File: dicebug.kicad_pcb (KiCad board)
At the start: 2 copper layers, 120.6 x 77.6 mm, 33 parts, among them SW1 SW_SPDT, U1 74LV163ADR, U3 74HCS7266DR, U5 iqs211a

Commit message: mostly done...
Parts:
- BT1: footprint Battery:BatteryHolder_Keystone_3034_1x20mm -> sensors:bh-3034-74-combined
- D1, D2, D3, D4, D5, D6, D7: footprint proj_footprints:PointLED_reverse_mount -> proj_footprints:PointLED_reverse_mount_bigger_pads
- TP2, TP3, TP4: footprint TestPoint:TestPoint_Pad_D2.0mm -> TestPoint:TestPoint_Pad_D1.0mm
- moved TP3 137.8 mm to (90.7, 100.3)
- moved TP2 119.2 mm to (108.6, 102.5)
- moved TP1 57.0 mm to (116.5, 95.2)
- moved TP4 42.9 mm to (92.5, 112.1)
- moved R1 5.16 mm to (93.0, 97.1), turned to 90 degrees
- moved R4 2.28 mm to (112.8, 95.2)
- moved BT1 1.25 mm to (100.1, 87.2), turned to 0 degrees
- moved C1 0.12 mm to (95.9, 103.0)
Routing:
- net GND: track 146.3 -> 186.6 mm
- net Net-(BT1-+): track 50.7 -> 70.2 mm
- net Net-(D1-A): track 3.85 -> 10.4 mm
- net Net-(U5-IO1/SCL): track 0.00 -> 5.26 mm
- net Net-(R4-Pad1): track 80.8 -> 76.5 mm
- net Net-(U1-Q0): track 38.4 -> 42.0 mm
- net Net-(R6-Pad1): track 42.9 -> 44.6 mm
- net +3V0: track 58.0 -> 59.3 mm
- net Net-(D4-A): track 3.05 -> 1.86 mm
- net Net-(R2-Pad1): track 83.4 -> 84.5 mm
- net Net-(U1-CP): track 15.0 -> 15.7 mm
- removed copper zone on B.Cu, net (none)
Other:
- board size 120.6 x 77.6 mm -> 47.8 x 48.5 mm
- board text added: "JLCJLCJLCJLC"

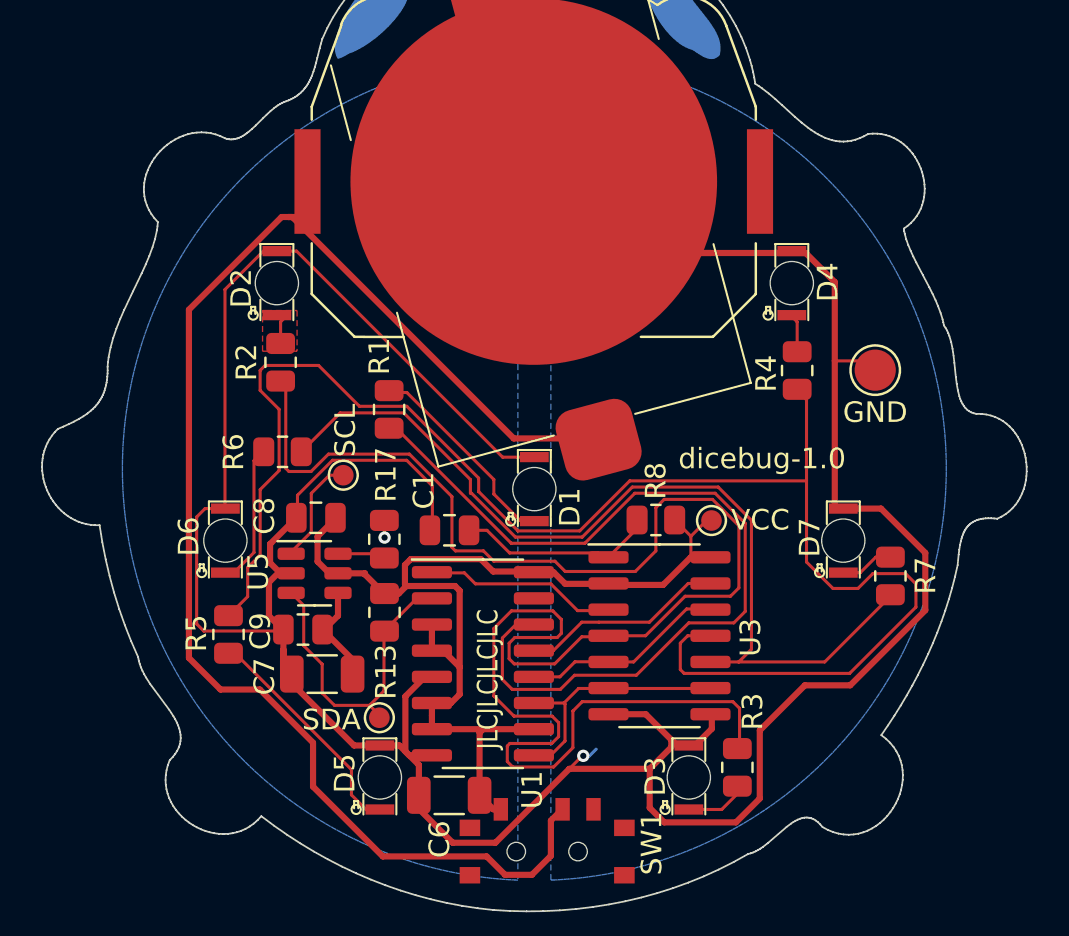
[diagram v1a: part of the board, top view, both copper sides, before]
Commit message: updated part values, numbers/id and manufacturers; added comments
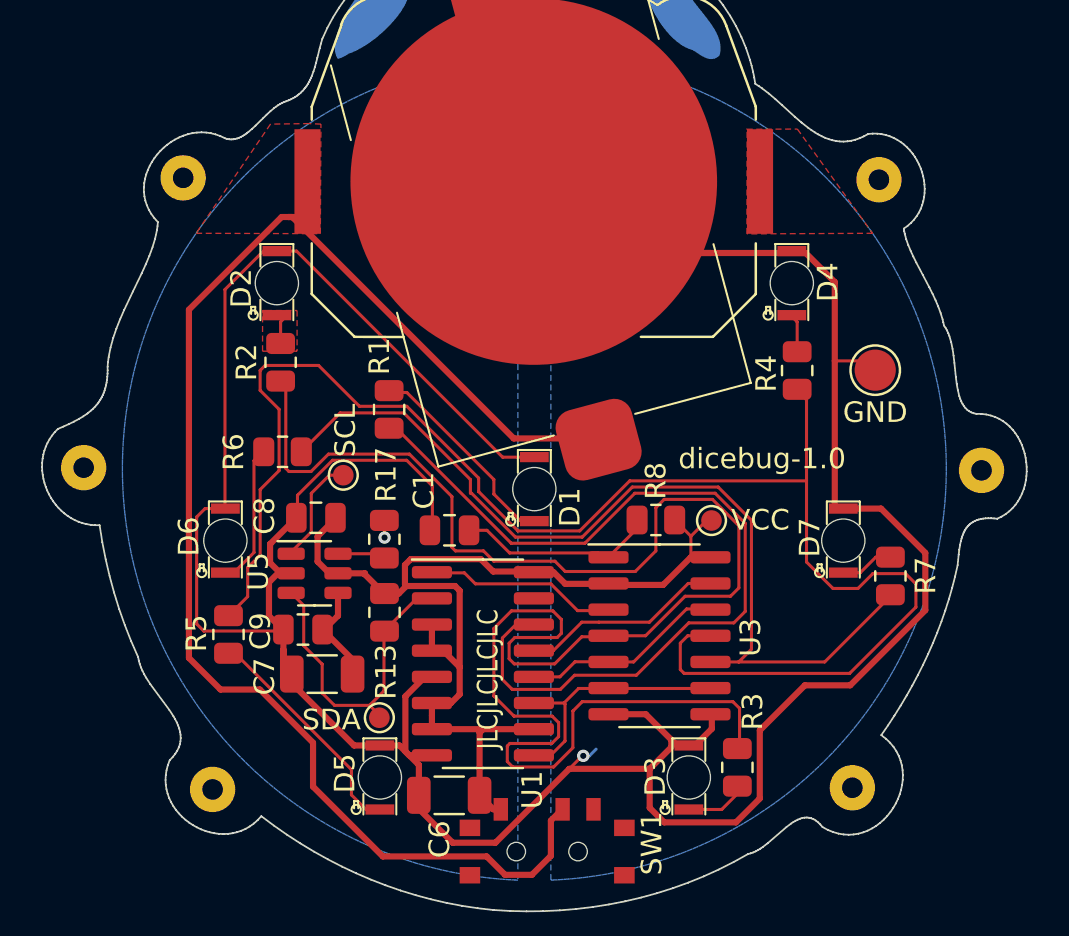
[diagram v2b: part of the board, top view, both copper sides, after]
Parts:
- added H1: Foot, sensors:foot, F.Cu at (116.7, 86.0)
- added H2: Foot, sensors:foot, F.Cu at (121.7, 100.1)
- added H3: Foot, sensors:foot, F.Cu at (115.4, 115.5)
- added H4: Foot, sensors:foot, F.Cu at (84.4, 115.6)
- added H5: Foot, sensors:foot, F.Cu at (78.1, 100.0)
- added H6: Foot, sensors:foot, F.Cu at (83.0, 85.9)
- R1, R2, R3, R4, R5, R6, R7: value 2k8 -> 4k7
- R17: value 470 -> 4k7
- U5: value iqs211a -> iqs211b
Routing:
- added copper zone on F.Cu, net Net-(BT1-+)

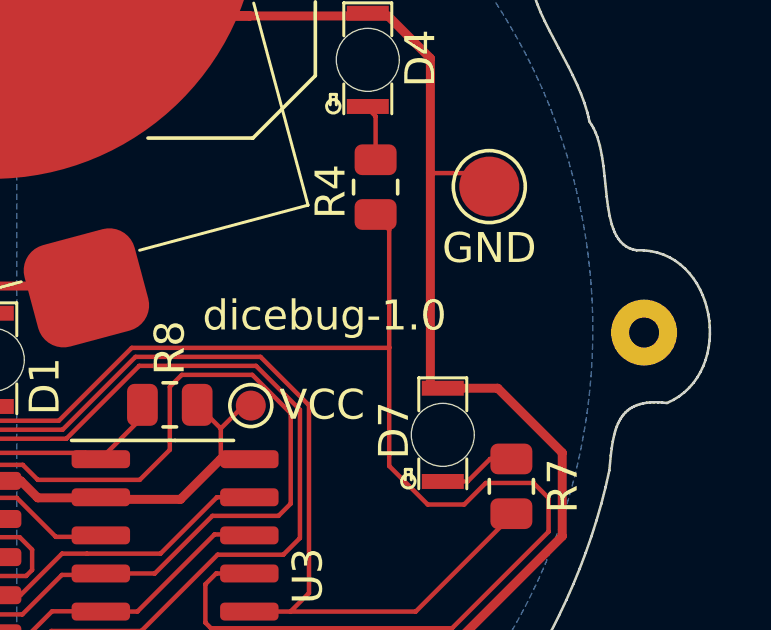
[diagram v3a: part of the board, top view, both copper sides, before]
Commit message: PCB: removed feet from paste layer.
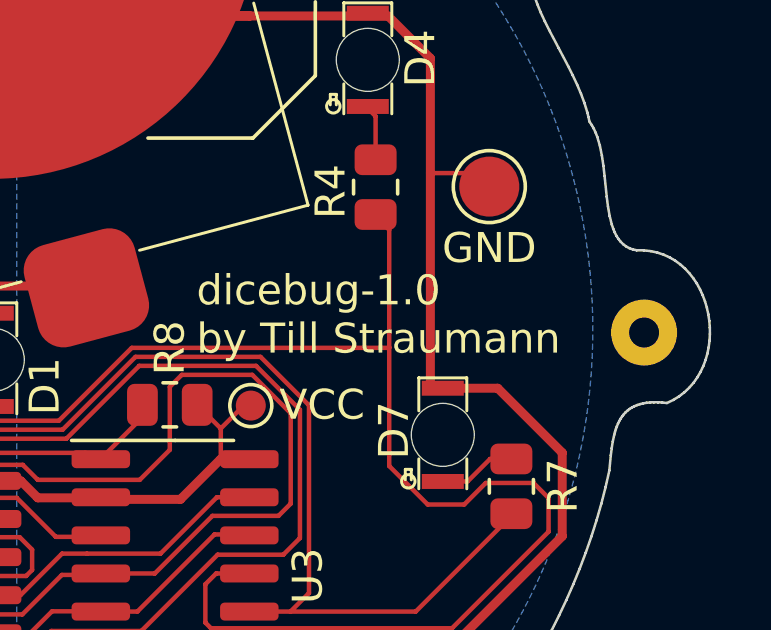
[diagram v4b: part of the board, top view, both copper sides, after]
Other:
- board text added: "dicebug-1.0 by Till Straumann"
- board text removed: "dicebug-1.0"
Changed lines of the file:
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@@
   )
   (paper "A4")
+  (title_block
+    (title "DiceBug")
+    (date "2023-05-30")
+    (rev "v1.0")
+    (company "Till Straumann; Artwork by Adam.")
+    (comment 1 "License: OHL-S/CC-BY-NC-ND; no warranty, express or implicit.")
+  )
   (layers
     (0 "F.Cu" signal)
@@
         (effects (font (size 1 1) (thickness 0.15)))
     )
-    (pad "1" thru_hole circle (at 0 0) (size 2.2 2.2) (drill 1) (layers "*.Cu" "F.Paste" "F.Mask"))
+    (pad "1" thru_hole circle (at 0 0) (size 2.2 2.2) (drill 1) (layers "*.Cu" "F.Mask"))
   )
   (footprint "Capacitor_SMD:C_1206_3216Metric" (layer "F.Cu")
@@
         (effects (font (size 1 1) (thickness 0.15)))
     )
-    (pad "1" thru_hole circle (at 0 0) (size 2.2 2.2) (drill 1) (layers "*.Cu" "F.Paste" "F.Mask"))
+    (pad "1" thru_hole circle (at 0 0) (size 2.2 2.2) (drill 1) (layers "*.Cu" "F.Mask"))
   )
   (footprint "sensors:bh-3034-74-combined" (layer "F.Cu")
@@
         (effects (font (size 1 1) (thickness 0.15)))
     )
-    (pad "1" thru_hole circle (at 0 0) (size 2.2 2.2) (drill 1) (layers "*.Cu" "F.Paste" "F.Mask"))
+    (pad "1" thru_hole circle (at 0 0) (size 2.2 2.2) (drill 1) (layers "*.Cu" "F.Mask"))
   )
   (footprint "Resistor_SMD:R_0805_2012Metric" (layer "F.Cu")
@@
         (effects (font (size 1 1) (thickness 0.15)))
     )
-    (pad "1" thru_hole circle (at 0 0) (size 2.2 2.2) (drill 1) (layers "*.Cu" "F.Paste" "F.Mask"))
+    (pad "1" thru_hole circle (at 0 0) (size 2.2 2.2) (drill 1) (layers "*.Cu" "F.Mask"))
   )
   (footprint "TestPoint:TestPoint_Pad_D2.0mm" (layer "F.Cu")
@@
         (effects (font (size 1 1) (thickness 0.15)))
     )
-    (pad "1" thru_hole circle (at 0 0) (size 2.2 2.2) (drill 1) (layers "*.Cu" "F.Paste" "F.Mask"))
+    (pad "1" thru_hole circle (at 0 0) (size 2.2 2.2) (drill 1) (layers "*.Cu" "F.Mask"))
   )
   (footprint "Package_SO:SOIC-14_3.9x8.7mm_P1.27mm" (layer "F.Cu")
@@
         (effects (font (size 1 1) (thickness 0.15)))
     )
-    (pad "1" thru_hole circle (at 0 0) (size 2.2 2.2) (drill 1) (layers "*.Cu" "F.Paste" "F.Mask"))
+    (pad "1" thru_hole circle (at 0 0) (size 2.2 2.2) (drill 1) (layers "*.Cu" "F.Mask"))
   )
   (footprint "Resistor_SMD:R_0805_2012Metric" (layer "F.Cu")
@@
   (gr_circle (center 85 115) (end 89 115)
     (stroke (width 0.153) (type default)) (fill none) (layer "B.Fab"))
-  (gr_text "dicebug-1.0" (at 106.99 100.11) (layer "F.SilkS")
+  (gr_text "dicebug-1.0\nby Till Straumann" (at 106.79 100.88) (layer "F.SilkS")
     (effects (font (size 1 1) (thickness 0.153)) (justify left bottom))
   )
